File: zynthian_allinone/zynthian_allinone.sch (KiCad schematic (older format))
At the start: 30 parts

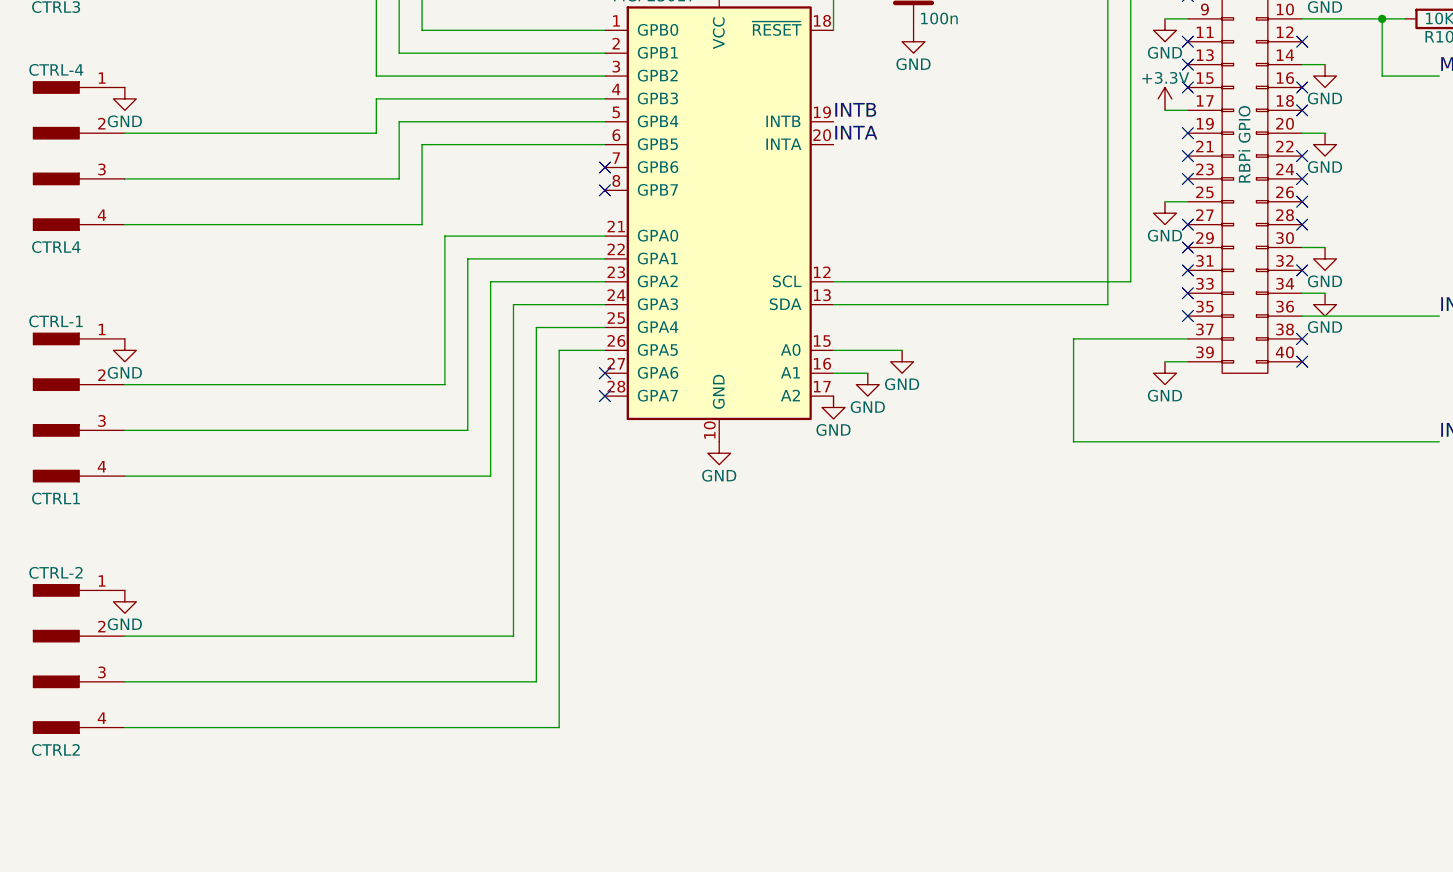
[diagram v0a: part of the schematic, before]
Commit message: Minor revisions of All-In-One circuit: Copper logos (using F.Mask layer) and new SW1 connector with 4 extra switches.
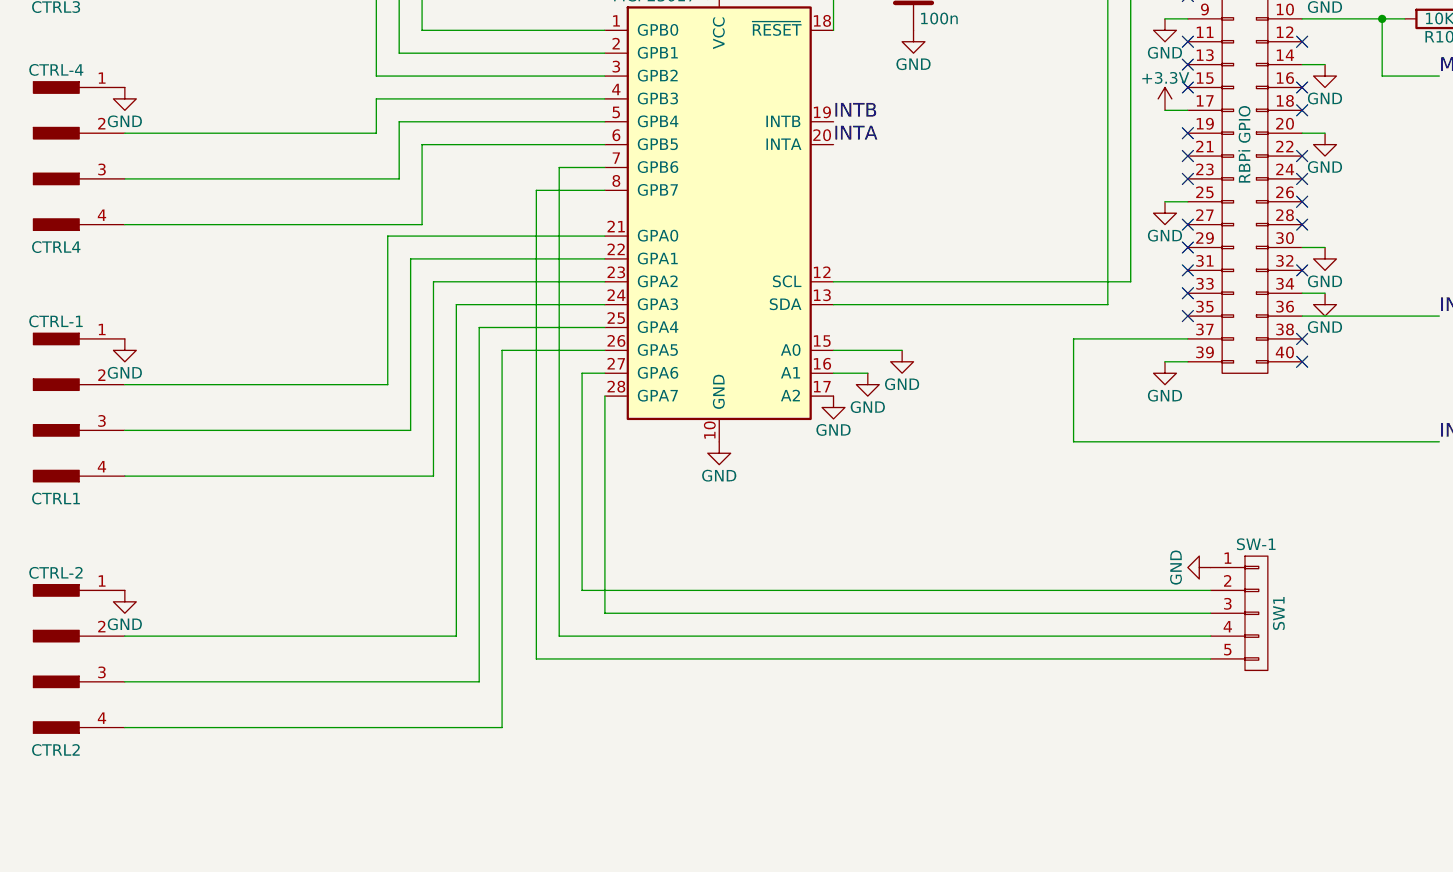
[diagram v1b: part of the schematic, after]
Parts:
- added SW-1: SW1, Connectors_JST:JST_XH_B05B-XH-A_05x2.50mm_Straight, symbol CONN_01X05
- D2: footprint Discret:D3 -> Discret:D4
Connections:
- net GND: now also SW-1.1 (P1)
- net at MCP23017.27 (GPA6): now also SW-1.2 (P2)
- net at MCP23017.28 (GPA7): now also SW-1.3 (P3)
- net at MCP23017.7 (GPB6): now also SW-1.4 (P4)
- net at MCP23017.8 (GPB7): now also SW-1.5 (P5)
- no-connect marks 26 -> 22
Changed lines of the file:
@@
 NoConn ~ 7000 5400
 NoConn ~ 7000 5100
-NoConn ~ 3950 4650
-NoConn ~ 3950 4750
-NoConn ~ 3950 5550
-NoConn ~ 3950 5650
 $Comp
 L PWR_FLAG #FLG017
@@
 F 0 "D2" H 13300 3800 50  0000 C CNN
 F 1 "1N5819" H 13300 3600 50  0000 C CNN
-F 2 "Discret:D3" H 13300 3700 50  0001 C CNN
+F 2 "Discret:D4" H 13300 3700 50  0001 C CNN
 F 3 "" H 13300 3700 50  0001 C CNN
 	1    13300 3700
@@
 	3150 4550 3950 4550
 Wire Wire Line
-	1850 5600 3250 5600
-Wire Wire Line
-	3250 5600 3250 4950
-Wire Wire Line
-	3250 4950 3950 4950
-Wire Wire Line
-	1850 5800 3350 5800
-Wire Wire Line
-	3350 5800 3350 5050
-Wire Wire Line
-	3350 5050 3950 5050
-Wire Wire Line
-	1850 6000 3450 6000
-Wire Wire Line
-	3450 6000 3450 5150
-Wire Wire Line
-	3450 5150 3950 5150
-Wire Wire Line
-	1850 6700 3550 6700
-Wire Wire Line
-	3550 6700 3550 5250
-Wire Wire Line
-	3550 5250 3950 5250
-Wire Wire Line
-	1850 6900 3650 6900
-Wire Wire Line
-	3650 6900 3650 5350
-Wire Wire Line
-	3650 5350 3950 5350
-Wire Wire Line
-	1850 7100 3750 7100
-Wire Wire Line
-	3750 7100 3750 5450
-Wire Wire Line
-	3750 5450 3950 5450
+	1850 5600 3000 5600
+Wire Wire Line
+	3000 5600 3000 4950
+Wire Wire Line
+	3000 4950 3950 4950
+Wire Wire Line
+	1850 5800 3100 5800
+Wire Wire Line
+	3100 5800 3100 5050
+Wire Wire Line
+	3100 5050 3950 5050
+Wire Wire Line
+	1850 6000 3200 6000
+Wire Wire Line
+	3200 6000 3200 5150
+Wire Wire Line
+	3200 5150 3950 5150
+Wire Wire Line
+	1850 6700 3300 6700
+Wire Wire Line
+	3300 6700 3300 5250
+Wire Wire Line
+	3300 5250 3950 5250
+Wire Wire Line
+	1850 6900 3400 6900
+Wire Wire Line
+	3400 6900 3400 5350
+Wire Wire Line
+	3400 5350 3950 5350
+Wire Wire Line
+	1850 7100 3500 7100
+Wire Wire Line
+	3500 7100 3500 5450
+Wire Wire Line
+	3500 5450 3950 5450
 Wire Wire Line
 	1850 3250 1900 3250
@@
 $EndComp
 Connection ~ 4950 3750
+$Comp
+L CONN_01X05 SW-1
+U 1 1 5B111921
+P 6800 6600
+F 0 "SW-1" H 6800 6900 50  0000 C CNN
+F 1 "SW1" V 6900 6600 50  0000 C CNN
+F 2 "Connectors_JST:JST_XH_B05B-XH-A_05x2.50mm_Straight" H 6800 6600 50  0001 C CNN
+F 3 "" H 6800 6600 50  0001 C CNN
+	1    6800 6600
+	1    0    0    -1
+$EndComp
+Wire Wire Line
+	3950 5650 3950 6600
+Wire Wire Line
+	3950 6600 6600 6600
+Wire Wire Line
+	3950 5550 3850 5550
+Wire Wire Line
+	3850 5550 3850 6500
+Wire Wire Line
+	3850 6500 6600 6500
+Wire Wire Line
+	3950 4650 3750 4650
+Wire Wire Line
+	3750 4650 3750 6700
+Wire Wire Line
+	3750 6700 6600 6700
+Wire Wire Line
+	3950 4750 3650 4750
+Wire Wire Line
+	3650 4750 3650 6800
+Wire Wire Line
+	3650 6800 6600 6800
+$Comp
+L GND #PWR042
+U 1 1 5B112FD7
+P 6600 6400
+F 0 "#PWR042" H 6600 6150 50  0001 C CNN
+F 1 "GND" H 6600 6250 50  0000 C CNN
+F 2 "" H 6600 6400 50  0001 C CNN
+F 3 "" H 6600 6400 50  0001 C CNN
+	1    6600 6400
+	0    1    1    0
+$EndComp
 $EndSCHEMATC

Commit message: + Add a MIDI standalone scheme on zynaptik v2. + Update kicad's cache & lib files for some projects.
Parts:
- C1, C2, C3, C4: symbol C -> zynthian_allinone-rescue:C
- CTRL-1, CTRL-2, CTRL-3, CTRL-4, MIDI-1, MIDI-2, MIDI-3: symbol CONN_01X04_MALE -> zynthian_allinone-rescue:CONN_01X04_MALE
- D1, D2, D3, D4: symbol D -> zynthian_allinone-rescue:D
- MCP23017: symbol MCP23017 -> zynthian_allinone-rescue:MCP23017
- OC1, OC2, OC3: symbol H11L1 -> zynthian_allinone-rescue:H11L1
- R1, R10, R2, R3, R4, R5, R6, R7, R8, R9: symbol R -> zynthian_allinone-rescue:R
- RBPi-1: symbol CONN_02X20 -> zynthian_allinone-rescue:CONN_02X20
- SW-1: symbol CONN_01X05 -> zynthian_allinone-rescue:CONN_01X05
